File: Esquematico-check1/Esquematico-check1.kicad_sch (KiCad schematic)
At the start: 22 parts, among them J1 Conn_01x02, J2 Conn_01x02, Q1 BC547, Q2 BC547, Q3 BC547, Q4 BC547, Q5 BC547, Q6 BC557, Q7 BC557, Q8 BC557, U1 TL431D

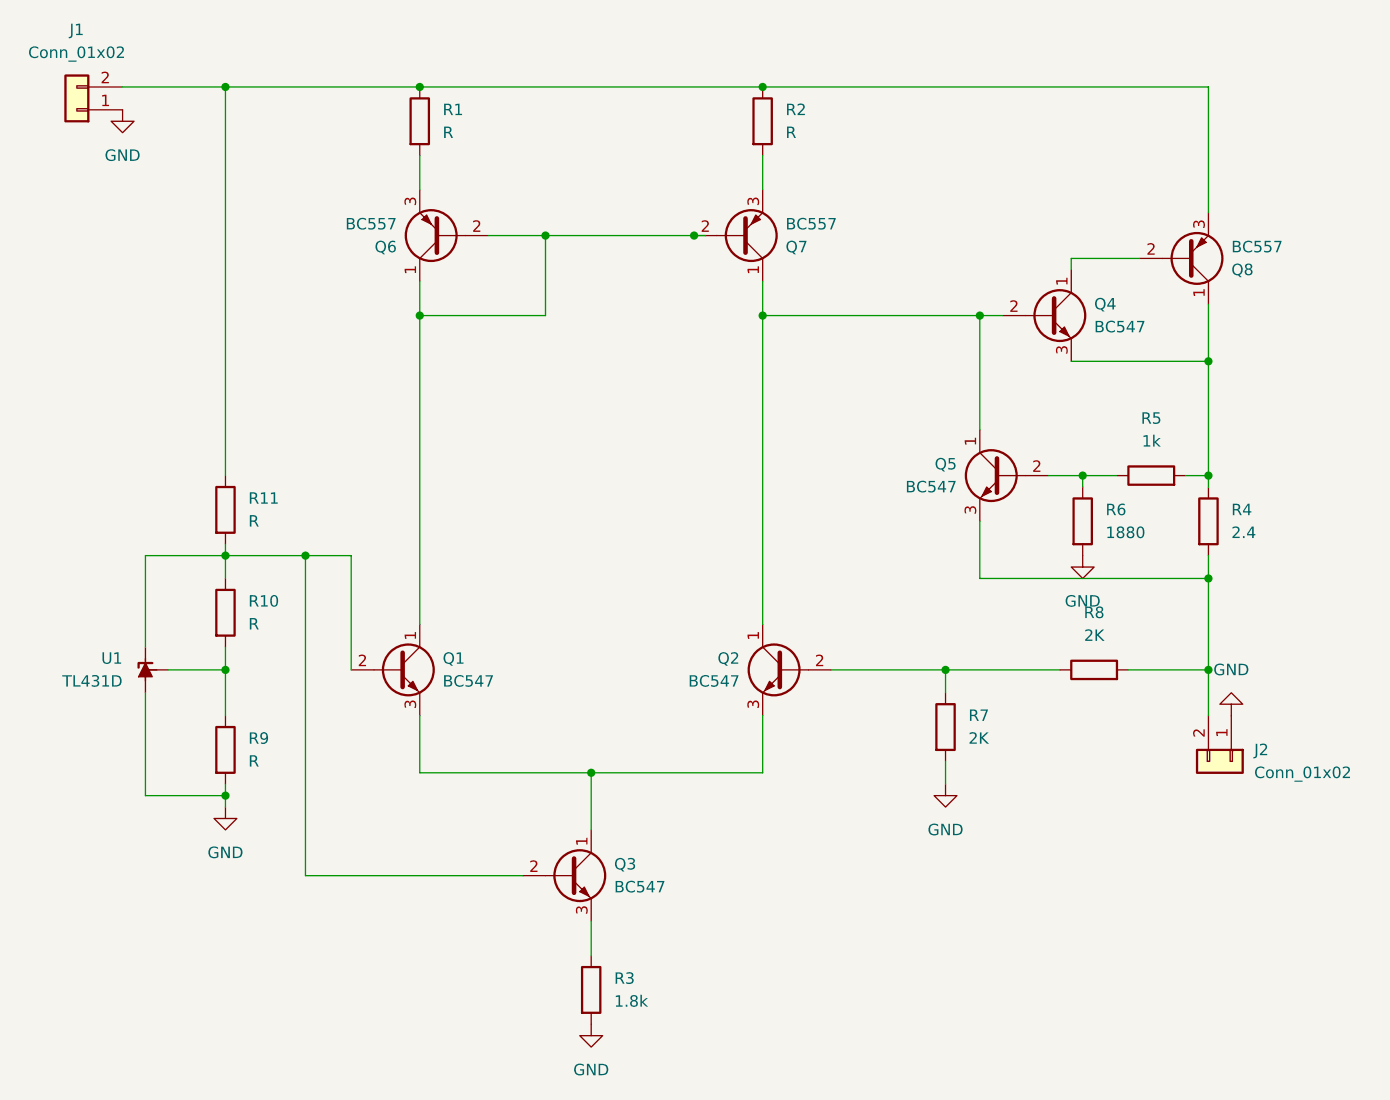
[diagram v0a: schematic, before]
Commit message: esquematico pcb, le falta la resistencia de la ref nomas
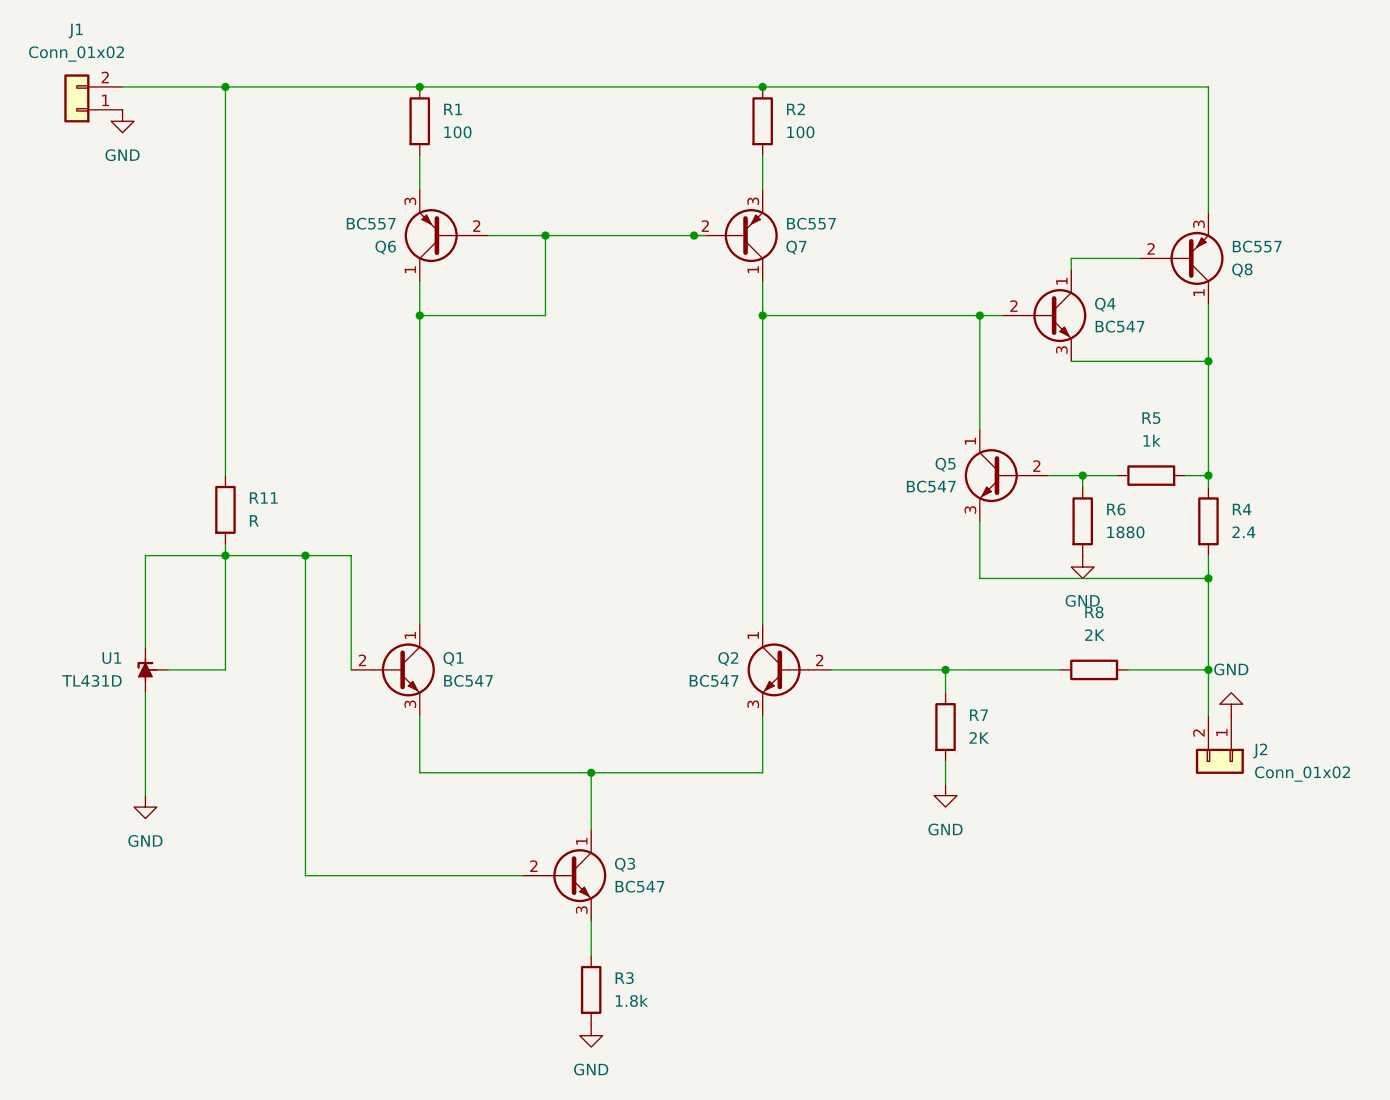
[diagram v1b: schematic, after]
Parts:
- removed R10, R9: R, symbol Device:R
- R1, R2: value R -> 100
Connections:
- net at U1.8 (REF): now also Q1.2 (B), Q3.2 (B), R11.2, U1.1 (K)
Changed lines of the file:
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@@
-	)
-	(junction
-		(at 80.01 129.54)
-		(diameter 0)
-		(color 0 0 0 0)
 	)
 	(junction
@@
 	)
 	(junction
-		(at 80.01 115.57)
-		(diameter 0)
-		(color 0 0 0 0)
-	)
-	(junction
 		(at 139.7 76.2)
 		(diameter 0)
@@
 	(wire
 		(pts
-			(xy 80.01 102.87) (xy 80.01 105.41)
-		)
-		(stroke
-			(width 0)
-			(type default)
-		)
-	)
-	(wire
-		(pts
 			(xy 173.99 81.28) (xy 189.23 81.28)
 		)
@@
 	(wire
 		(pts
-			(xy 80.01 129.54) (xy 71.12 129.54)
-		)
-		(stroke
-			(width 0)
-			(type default)
-		)
-	)
-	(wire
-		(pts
 			(xy 189.23 81.28) (xy 189.23 74.93)
 		)
@@
 	(wire
 		(pts
-			(xy 80.01 113.03) (xy 80.01 115.57)
-		)
-		(stroke
-			(width 0)
-			(type default)
-		)
-	)
-	(wire
-		(pts
 			(xy 175.26 93.98) (xy 175.26 95.25)
 		)
@@
 	(wire
 		(pts
+			(xy 80.01 102.87) (xy 80.01 115.57)
+		)
+		(stroke
+			(width 0)
+			(type default)
+		)
+	)
+	(wire
+		(pts
 			(xy 120.65 127) (xy 101.6 127)
 		)
@@
 	(wire
 		(pts
+			(xy 73.66 115.57) (xy 80.01 115.57)
+		)
+		(stroke
+			(width 0)
+			(type default)
+		)
+	)
+	(wire
+		(pts
 			(xy 189.23 64.77) (xy 189.23 50.8)
 		)
@@
 	(wire
 		(pts
-			(xy 80.01 115.57) (xy 80.01 120.65)
-		)
-		(stroke
-			(width 0)
-			(type default)
-		)
-	)
-	(wire
-		(pts
-			(xy 80.01 130.81) (xy 80.01 129.54)
-		)
-		(stroke
-			(width 0)
-			(type default)
-		)
-	)
-	(wire
-		(pts
 			(xy 101.6 76.2) (xy 101.6 110.49)
 		)
@@
 	(wire
 		(pts
-			(xy 73.66 115.57) (xy 80.01 115.57)
-		)
-		(stroke
-			(width 0)
-			(type default)
-		)
-	)
-	(wire
-		(pts
 			(xy 163.83 76.2) (xy 166.37 76.2)
 		)
@@
 	(wire
 		(pts
-			(xy 80.01 129.54) (xy 80.01 128.27)
-		)
-		(stroke
-			(width 0)
-			(type default)
-		)
-	)
-	(wire
-		(pts
 			(xy 163.83 105.41) (xy 189.23 105.41)
 		)
@@
 			(width 0)
 			(type default)
-		)
-	)
-	(symbol
-		(lib_id "Device:R")
-		(at 80.01 124.46 0)
-		(unit 1)
-		(exclude_from_sim no)
-		(in_bom yes)
-		(on_board yes)
-		(dnp no)
-		(fields_autoplaced yes)
-		(property "Reference" "R9"
-			(at 82.55 123.1899 0)
-			(effects
-				(font
-					(size 1.27 1.27)
-				)
-				(justify left)
-			)
-		)
-		(property "Value" "R"
-			(at 82.55 125.7299 0)
-			(effects
-				(font
-					(size 1.27 1.27)
-				)
-				(justify left)
-			)
-		)
-		(property "Footprint" ""
-			(at 78.232 124.46 90)
-			(effects
-				(font
-					(size 1.27 1.27)
-				)
-				(hide yes)
-			)
-		)
-		(property "Datasheet" "~"
-			(at 80.01 124.46 0)
-			(effects
-				(font
-					(size 1.27 1.27)
-				)
-				(hide yes)
-			)
-		)
-		(property "Description" "Resistor"
-			(at 80.01 124.46 0)
-			(effects
-				(font
-					(size 1.27 1.27)
-				)
-				(hide yes)
-			)
-		)
-		(pin "2"
-		)
-		(pin "1"
-		)
-		(instances
-			(project "Esquematico-check1"
-				(path "/f9400a4d-2b42-400b-b70b-8f58c3eb7ffc"
-					(reference "R9")
-					(unit 1)
-				)
-			)
 		)
 	)
@@
 	)
 	(symbol
-		(lib_id "power:GND")
-		(at 80.01 130.81 0)
-		(unit 1)
-		(exclude_from_sim no)
-		(in_bom yes)
-		(on_board yes)
-		(dnp no)
-		(fields_autoplaced yes)
-		(property "Reference" "#PWR06"
-			(at 80.01 137.16 0)
-			(effects
-				(font
-					(size 1.27 1.27)
-				)
-				(hide yes)
-			)
-		)
-		(property "Value" "GND"
-			(at 80.01 135.89 0)
-			(effects
-				(font
-					(size 1.27 1.27)
-				)
-			)
-		)
-		(property "Footprint" ""
-			(at 80.01 130.81 0)
-			(effects
-				(font
-					(size 1.27 1.27)
-				)
-				(hide yes)
-			)
-		)
-		(property "Datasheet" ""
-			(at 80.01 130.81 0)
-			(effects
-				(font
-					(size 1.27 1.27)
-				)
-				(hide yes)
-			)
-		)
-		(property "Description" "Power symbol creates a global label with name \"GND\" , ground"
-			(at 80.01 130.81 0)
-			(effects
-				(font
-					(size 1.27 1.27)
-				)
-				(hide yes)
-			)
-		)
-		(pin "1"
-		)
-		(instances
-			(project "Esquematico-check1"
-				(path "/f9400a4d-2b42-400b-b70b-8f58c3eb7ffc"
-					(reference "#PWR06")
-					(unit 1)
-				)
-			)
-		)
-	)
-	(symbol
 		(lib_id "Transistor_BJT:BC547")
 		(at 142.24 115.57 0)
@@
 	)
 	(symbol
+		(lib_id "power:GND")
+		(at 71.12 129.54 0)
+		(unit 1)
+		(exclude_from_sim no)
+		(in_bom yes)
+		(on_board yes)
+		(dnp no)
+		(fields_autoplaced yes)
+		(property "Reference" "#PWR06"
+			(at 71.12 135.89 0)
+			(effects
+				(font
+					(size 1.27 1.27)
+				)
+				(hide yes)
+			)
+		)
+		(property "Value" "GND"
+			(at 71.12 134.62 0)
+			(effects
+				(font
+					(size 1.27 1.27)
+				)
+			)
+		)
+		(property "Footprint" ""
+			(at 71.12 129.54 0)
+			(effects
+				(font
+					(size 1.27 1.27)
+				)
+				(hide yes)
+			)
+		)
+		(property "Datasheet" ""
+			(at 71.12 129.54 0)
+			(effects
+				(font
+					(size 1.27 1.27)
+				)
+				(hide yes)
+			)
+		)
+		(property "Description" "Power symbol creates a global label with name \"GND\" , ground"
+			(at 71.12 129.54 0)
+			(effects
+				(font
+					(size 1.27 1.27)
+				)
+				(hide yes)
+			)
+		)
+		(pin "1"
+		)
+		(instances
+			(project ""
+				(path "/f9400a4d-2b42-400b-b70b-8f58c3eb7ffc"
+					(reference "#PWR06")
+					(unit 1)
+				)
+			)
+		)
+	)
+	(symbol
 		(lib_id "Transistor_BJT:BC547")
 		(at 171.45 76.2 0)
@@
 			)
 		)
-		(property "Value" "R"
+		(property "Value" "100"
 			(at 104.14 55.8799 0)
 			(effects
@@
 			)
 		)
-		(property "Value" "R"
+		(property "Value" "100"
 			(at 142.24 55.8799 0)
 			(effects
@@
 					(unit 1)
 				)
-			)
-		)
-	)
-	(symbol
-		(lib_id "Device:R")
-		(at 80.01 109.22 0)
-		(unit 1)
-		(exclude_from_sim no)
-		(in_bom yes)
-		(on_board yes)
-		(dnp no)
-		(fields_autoplaced yes)
-		(property "Reference" "R10"
-			(at 82.55 107.9499 0)
-			(effects
-				(font
-					(size 1.27 1.27)
-				)
-				(justify left)
-			)
-		)
-		(property "Value" "R"
-			(at 82.55 110.4899 0)
-			(effects
-				(font
-					(size 1.27 1.27)
-				)
-				(justify left)
-			)
-		)
-		(property "Footprint" ""
-			(at 78.232 109.22 90)
-			(effects
-				(font
-					(size 1.27 1.27)
-				)
-				(hide yes)
-			)
-		)
-		(property "Datasheet" "~"
-			(at 80.01 109.22 0)
-			(effects
-				(font
-					(size 1.27 1.27)
-				)
-				(hide yes)
-			)
-		)
-		(property "Description" "Resistor"
-			(at 80.01 109.22 0)
-			(effects
-				(font
-					(size 1.27 1.27)
-				)
-				(hide yes)
-			)
-		)
-		(pin "2"
-		)
-		(pin "1"
-		)
-		(instances
-			(project "Esquematico-check1"
-				(path "/f9400a4d-2b42-400b-b70b-8f58c3eb7ffc"
-					(reference "R10")
-					(unit 1)
-				)

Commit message: esquematico chk1 terminado
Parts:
- Q4: renamed from Q6; value BC557 -> BC547
- Q5: renamed from Q7; value BC557 -> BC547
- Q6: renamed from Q8; value BC557 -> MJE2955T
- R8: renamed from R11; value R -> 1k
- renumbered Q4 to Q3, Q5 to Q7, Q3 to Q8, R3 to R1, R8 to R2, R7 to R3, R5 to R4, R6 to R5, R1 to R6, R2 to R7, R4 to Rs
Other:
- moved on the sheet: J1, J2, Q1, Q2, Q3, Q4, Q5, Q6, Q7, Q8, R1, R2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

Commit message: ahora si el esquematico chk1
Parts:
- Q4, Q5: value BC547 -> BC557
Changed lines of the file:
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@@
 			)
 		)
-		(property "Value" "BC547"
+		(property "Value" "BC557"
 			(at 142.24 78.7401 0)
 			(effects
@@
 		(dnp no)
 		(property "Reference" "Q2"
-			(at 137.16 104.1399 0)
+			(at 136.652 108.712 0)
 			(effects
 				(font
@@
 		)
 		(property "Value" "BC547"
-			(at 137.16 106.6799 0)
+			(at 136.652 111.252 0)
 			(effects
 				(font
@@
 			)
 		)
-		(property "Value" "BC547"
+		(property "Value" "BC557"
 			(at 114.3 78.7401 0)
 			(effects
